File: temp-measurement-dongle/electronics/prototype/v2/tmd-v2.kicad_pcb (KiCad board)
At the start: 2 copper layers, 70.5 x 68.5 mm, 67 parts, among them J1 USB2UART, J2 1.47 IPS LCD, J3 ConnBattery, J5 lcd jumper, J6 lcd jumper, J7 lcd jumper, J8 RTD_PT100, Q1 SS8050, Q2 SS8050, Q3 SS8050, SW1 RST, SW3 Boot, SW9 PS Joystick, U1 CH340C, U2 ESP32-S3-WROOM-1, U3 TPS63001_SEPIC_3V3, U4 MAX31865xTP, U5 BQ24075RGT_DPPM

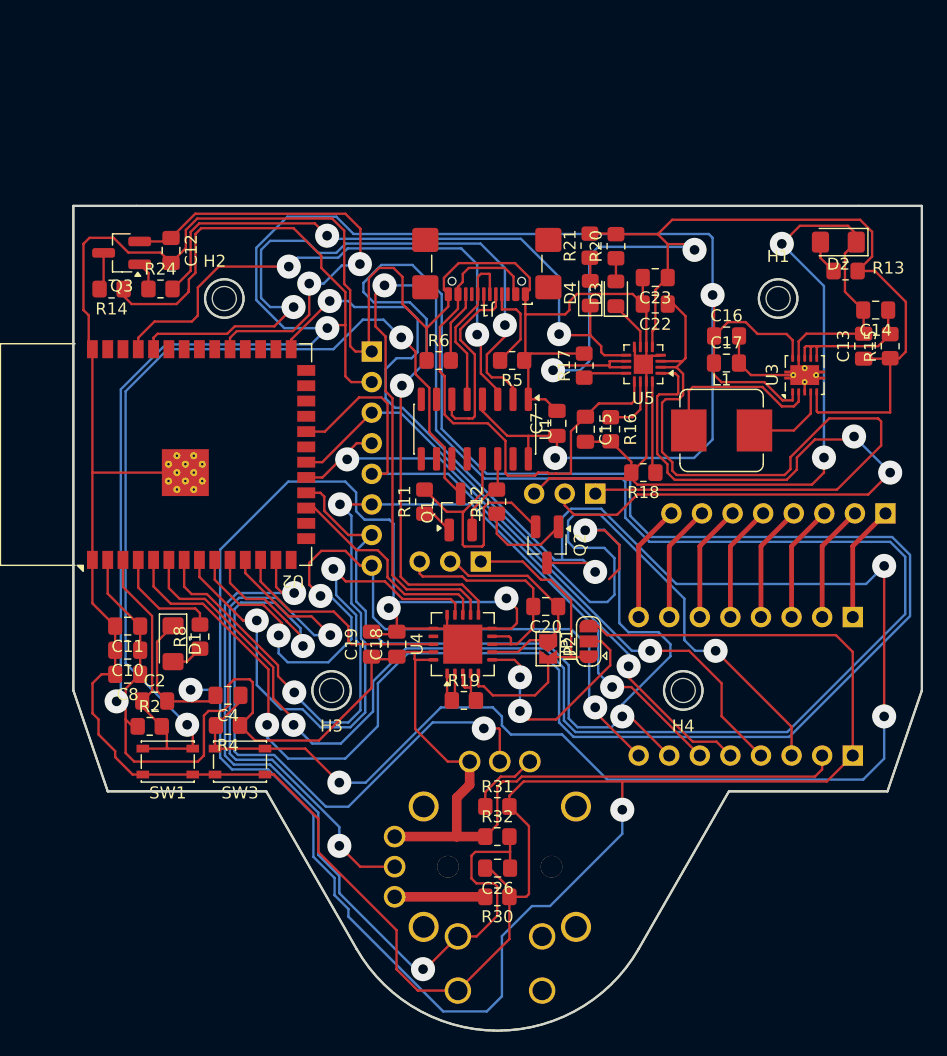
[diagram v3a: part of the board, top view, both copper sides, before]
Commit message: change board shape
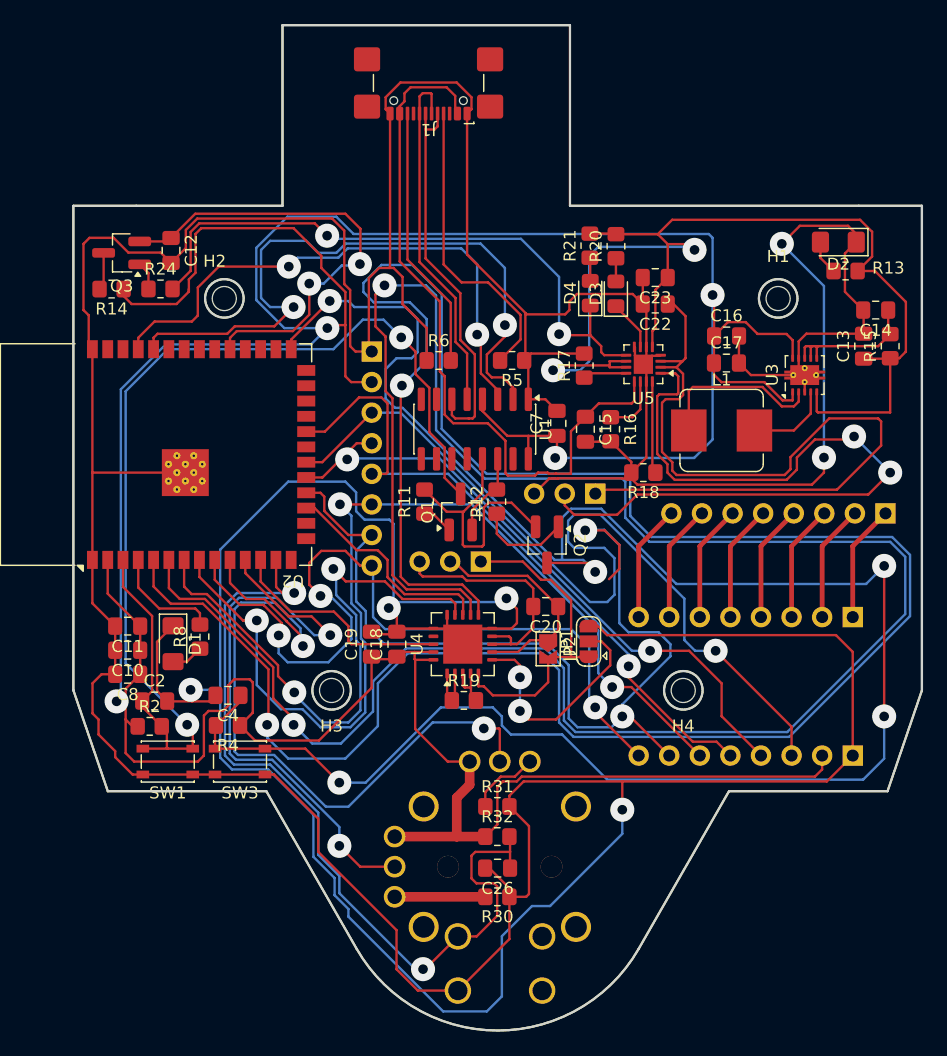
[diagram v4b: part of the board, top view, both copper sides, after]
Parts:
- moved J1 15.8 mm to (138.7, 55.5)
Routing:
- net GND: track 530.4 -> 556.7 mm
- net Net-(J1-CC1): track 7.55 -> 25.1 mm
- net Net-(J1-CC2): track 6.02 -> 22.0 mm
- net VBUS: track 44.6 -> 60.4 mm
- net Net-(U1-UD+): track 14.1 -> 29.6 mm
- net Net-(U1-UD-): track 17.2 -> 32.4 mm
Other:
- board size 70.5 x 68.5 mm -> 70.5 x 83.5 mm
